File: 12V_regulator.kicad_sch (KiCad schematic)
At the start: 39 parts, among them M1 -, M2 -, M3 -, M4 -, U11 XLM51772RHAR

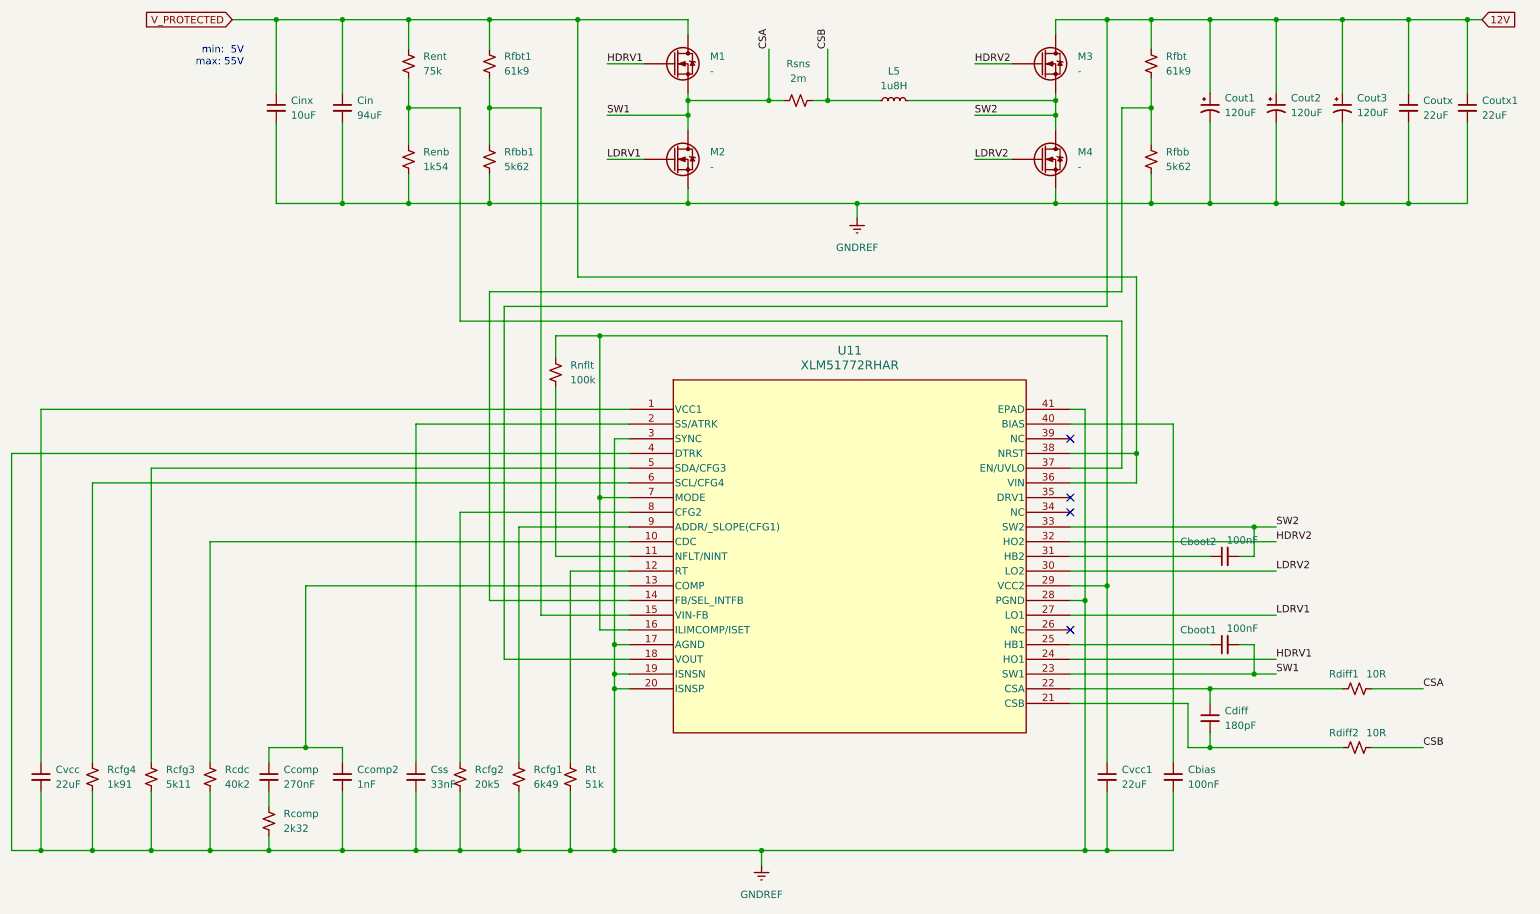
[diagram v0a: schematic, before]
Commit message: updated components and nets
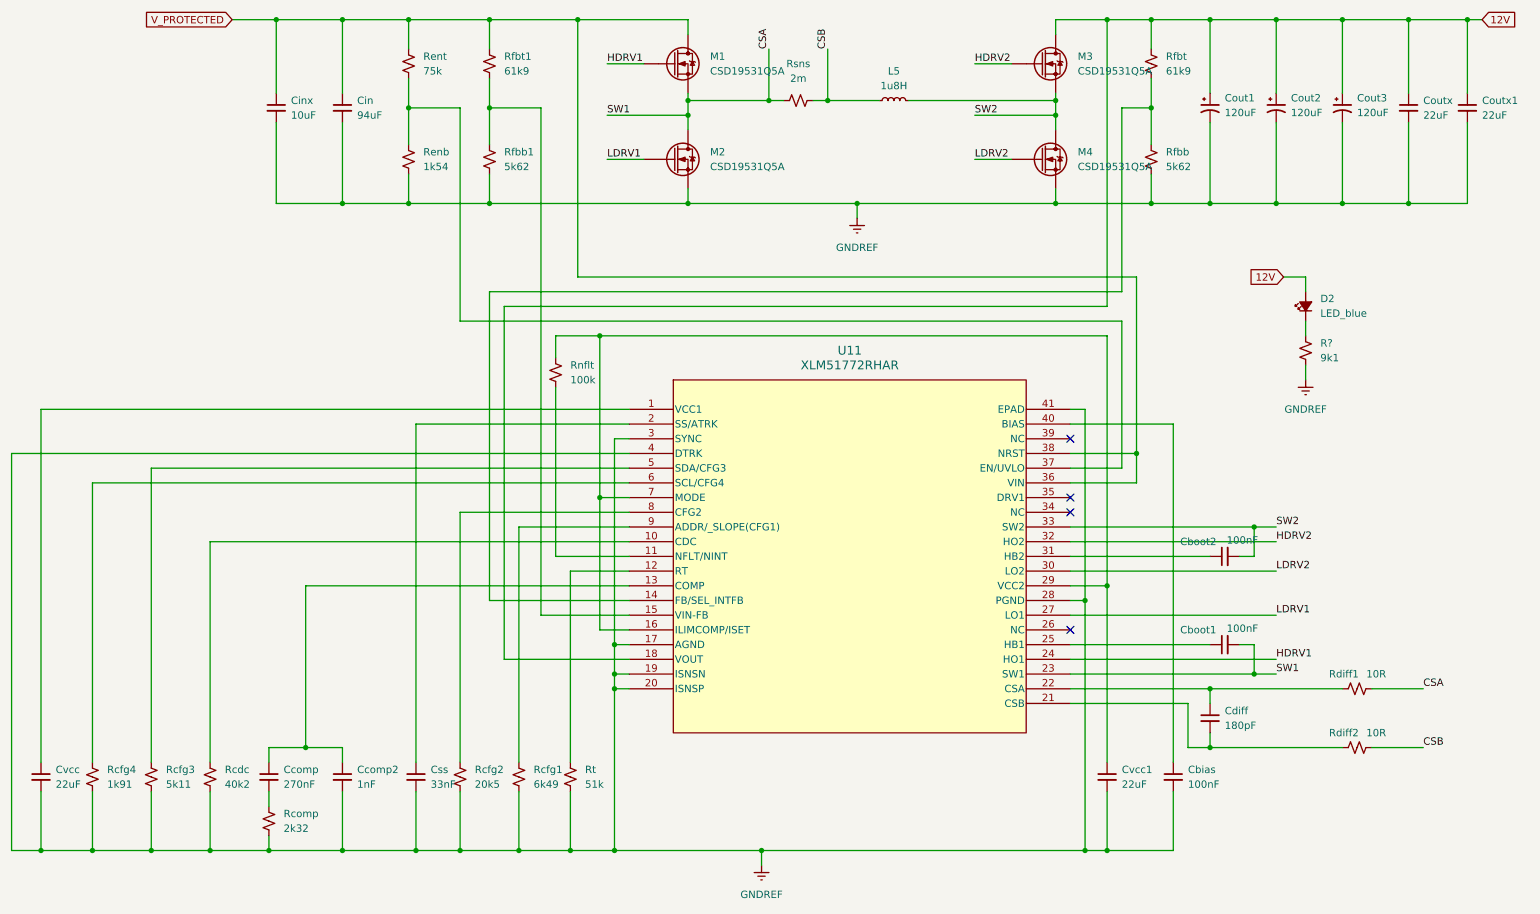
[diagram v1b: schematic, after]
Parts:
- added D2: LED_blue, symbol Device:LED_Small_Filled
- added R?: 9k1, symbol Device:R_Small_US
- M1, M2, M3, M4: value - -> CSD19531Q5A
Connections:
- net 12V: now also D2.2 (A)
- net GNDREF: now also R?.2
- new net: D2.1 (K), R?.1
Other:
- note removed: "min: 5V max: 55V"
